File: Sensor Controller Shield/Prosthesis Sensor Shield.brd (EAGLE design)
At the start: 101.6 x 53.3 mm, 46 parts, among them M1_ACT M02PTH, M2_ACT M02PTH

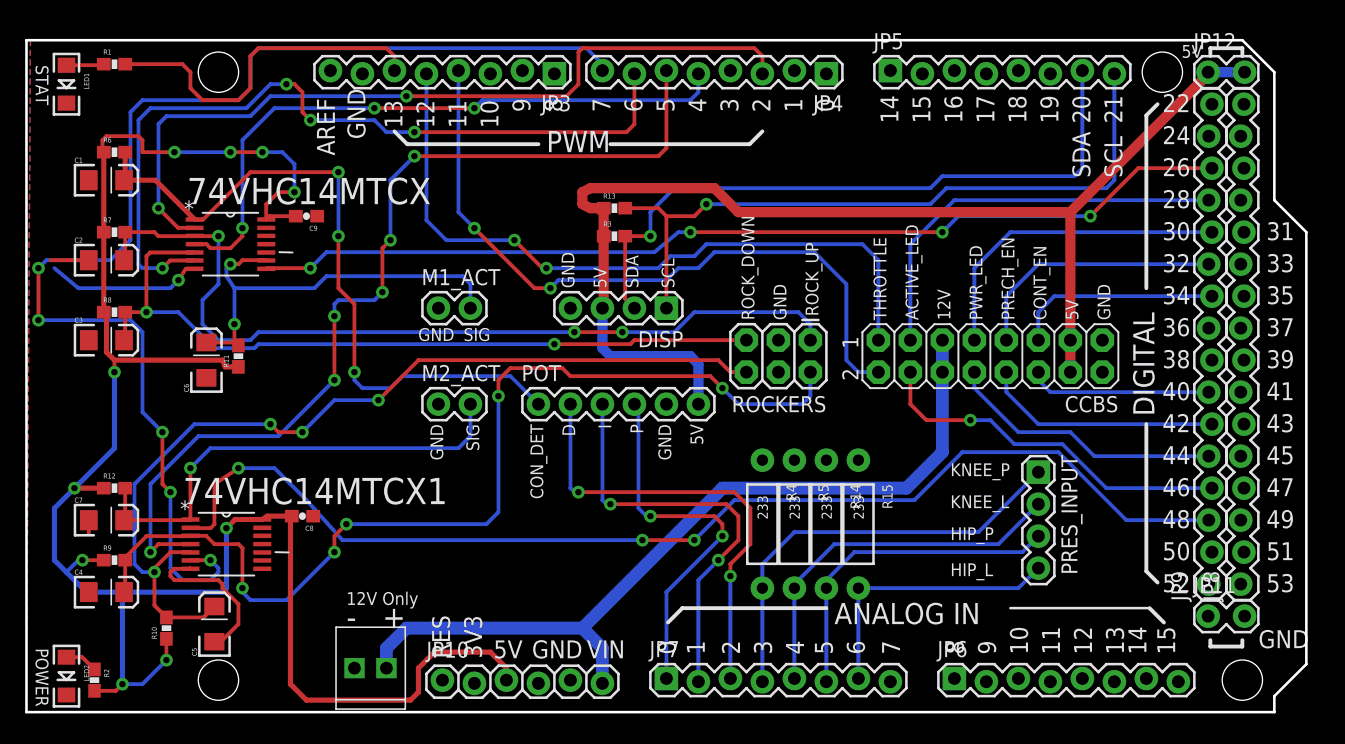
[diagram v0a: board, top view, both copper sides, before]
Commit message: Moved MCB titles to places layer from names
Cleared sensor shield of all components
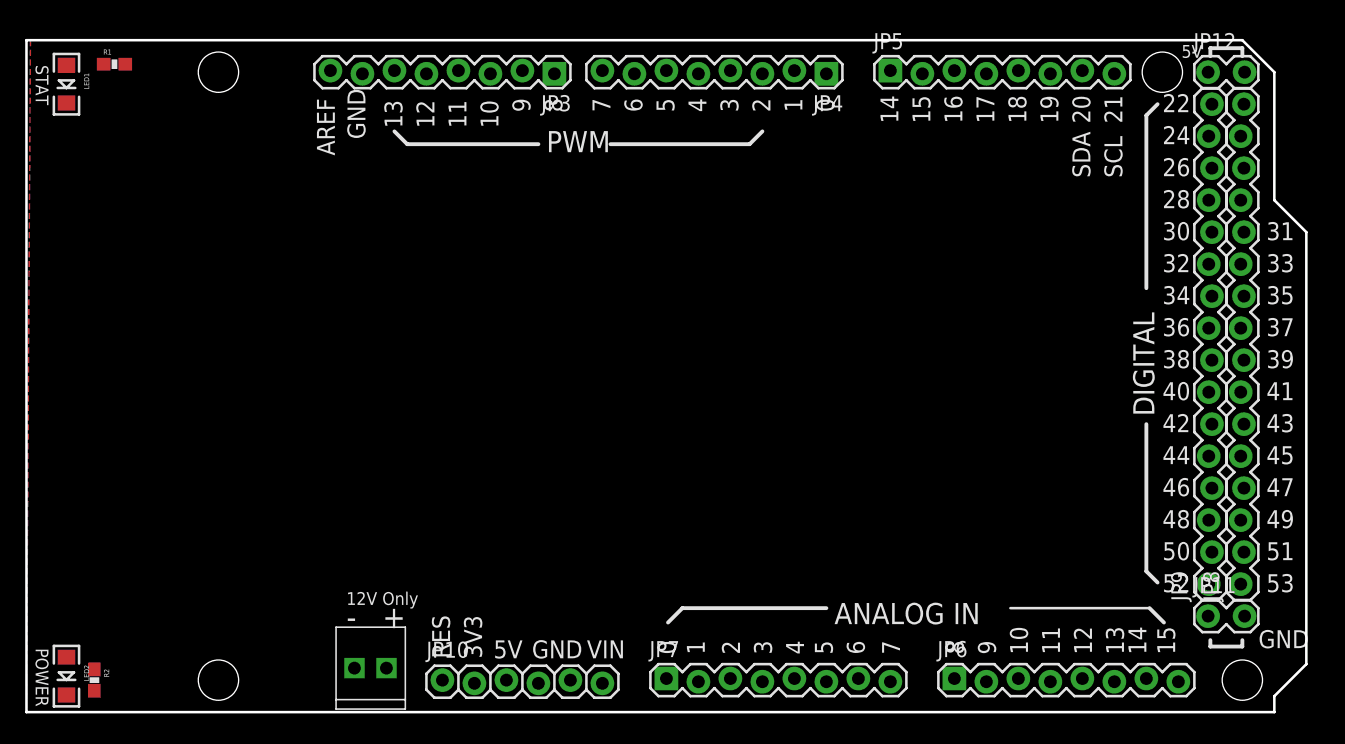
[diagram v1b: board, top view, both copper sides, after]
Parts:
- removed 74VHC14MTCX, 74VHC14MTCX1: 74VHC14MTCX, Fairchild_By_element14_Batch_1:SOP65P640X120-14N
- removed C1, C2, C3, C4, C5: 0.1uF, SparkFun-Capacitors:EIA3216
- removed C6, C7: (no value), SparkFun-Capacitors:EIA3216
- removed C8, C9: 0.1uF, SparkFun-Capacitors:0603-CAP
- removed CCBS: M08X2, SparkFun-Connectors:2X8
- removed DISP, PRES_INPUT: (no value), SparkFun-Connectors:1X04
- removed M1_ACT, M2_ACT: M02PTH, SparkFun-Connectors:1X02
- removed POT: (no value), SparkFun-Connectors:1X06
- removed R10, R6, R7, R8, R9: 1M, SparkFun-Resistors:0603-RES
- removed R11, R12: (no value), SparkFun-Resistors:0603-RES
- removed R13, R3: 3k, SparkFun-Resistors:0603-RES
- removed R14, R15, R4, R5: 233, SparkFun-Resistors:AXIAL-0.4
- removed ROCKERS: (no value), SparkFun-Connectors:2X3
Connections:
- removed net CON_DET: 74VHC14MTCX.1, C1.A, POT.1, R6.2
- removed net M1_ACT_SIG: 74VHC14MTCX.9, C6.A, M1_ACT.2, R11.2
- removed net M2_ACT_SIG: 74VHC14MTCX1.1, C7.A, M2_ACT.2, R12.2
- removed net MOT1_ROCK_DOWN: 74VHC14MTCX.5, C3.A, R8.2, ROCKERS.5
- removed net MOT1_ROCK_UP: 74VHC14MTCX.3, C2.A, R7.2, ROCKERS.1
- removed net MOT2_ROCK_DOWN: 74VHC14MTCX1.5, C5.A, R10.2, ROCKERS.6
- removed net MOT2_ROCK_UP: 74VHC14MTCX1.3, C4.A, R9.2, ROCKERS.2
- net 5V: no longer 74VHC14MTCX.14, 74VHC14MTCX1.14, C8.2, C9.2, R10.1, R11.1, R12.1, R6.1, R7.1, R8.1, R9.1
- net 5V@1: no longer CCBS.3, CCBS.4, DISP.3, POT.6, R13.1, R3.1
- net A0: no longer POT.4
- net A1: no longer POT.3
- net A2: no longer POT.2
- net A3: no longer PRES_INPUT.1, R4.P$2
- net A4: no longer PRES_INPUT.2, R5.P$2
- net A5: no longer PRES_INPUT.3, R14.P$2
- net A6: no longer PRES_INPUT.4, R15.P$2
- net D11: no longer CCBS.16
- net D12: no longer CCBS.15
- net D2: no longer 74VHC14MTCX.2
- net D26: no longer 74VHC14MTCX.8
- net D28: no longer CCBS.13
- net D30: no longer CCBS.9
- net D32: no longer CCBS.7
- net D34: no longer CCBS.5
- net D4: no longer 74VHC14MTCX.4
- net D40: no longer CCBS.6
- net D42: no longer CCBS.8
- net D44: no longer CCBS.10
- net D46: no longer CCBS.14
- net D48: no longer 74VHC14MTCX1.2
- net D5: no longer 74VHC14MTCX1.4
- net D6: no longer 74VHC14MTCX.6
- net D7: no longer 74VHC14MTCX1.6
- net GND: no longer 74VHC14MTCX.7, 74VHC14MTCX1.7, C1.C, C2.C, C3.C, C4.C, C5.C, C6.C, C7.C, C8.1, C9.1, CCBS.1, CCBS.2, DISP.4, M1_ACT.1, M2_ACT.1, POT.5, R14.P$1, R15.P$1, R4.P$1, R5.P$1, ROCKERS.3, ROCKERS.4
- net SCL: no longer DISP.1, R13.2
- net SDA: no longer DISP.2, R3.2
- net VIN: no longer CCBS.11, CCBS.12
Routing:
- net 5V: track 153.0 -> 0.00 mm, vias 10 -> 0
- net D7: track 100.2 -> 0.00 mm, vias 5 -> 0
- net 5V@1: track 96.0 -> 0.00 mm
- net D48: track 92.1 -> 0.00 mm, vias 3 -> 0
- net MOT2_ROCK_UP: track 79.9 -> 0.00 mm, vias 5 -> 0
- net D26: track 78.3 -> 0.00 mm, vias 4 -> 0
- net D5: track 75.4 -> 0.00 mm, vias 6 -> 0
- net MOT2_ROCK_DOWN: track 73.7 -> 0.00 mm, vias 4 -> 0
- net MOT1_ROCK_UP: track 68.7 -> 0.00 mm, vias 3 -> 0
- net VIN: track 66.1 -> 0.00 mm
- net D2: track 63.8 -> 0.00 mm, vias 2 -> 0
- net D6: track 63.6 -> 0.00 mm, vias 4 -> 0
- net MOT1_ROCK_DOWN: track 61.4 -> 0.00 mm, vias 2 -> 0
- net D12: track 56.7 -> 0.00 mm, vias 2 -> 0
- net SCL: track 56.0 -> 0.00 mm, vias 1 -> 0
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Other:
- board text removed: "12V"
- board text removed: "ACTIVE_LED"
- board text removed: "CONT_EN"
- board text removed: "CON_DET"
- board text removed: "D"
- board text removed: "HIP_L"
- board text removed: "HIP_P"
- board text removed: "I"
- board text removed: "KNEE_L"
- board text removed: "KNEE_P"
- board text removed: "P"
- board text removed: "PRECH_EN"
- board text removed: "PWR_LED"
- board text removed: "ROCK_DOWN"
- board text removed: "ROCK_UP"
- board text removed: "SIG"
- board text removed: "THROTTLE"
